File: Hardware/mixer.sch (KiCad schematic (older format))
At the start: 0 parts

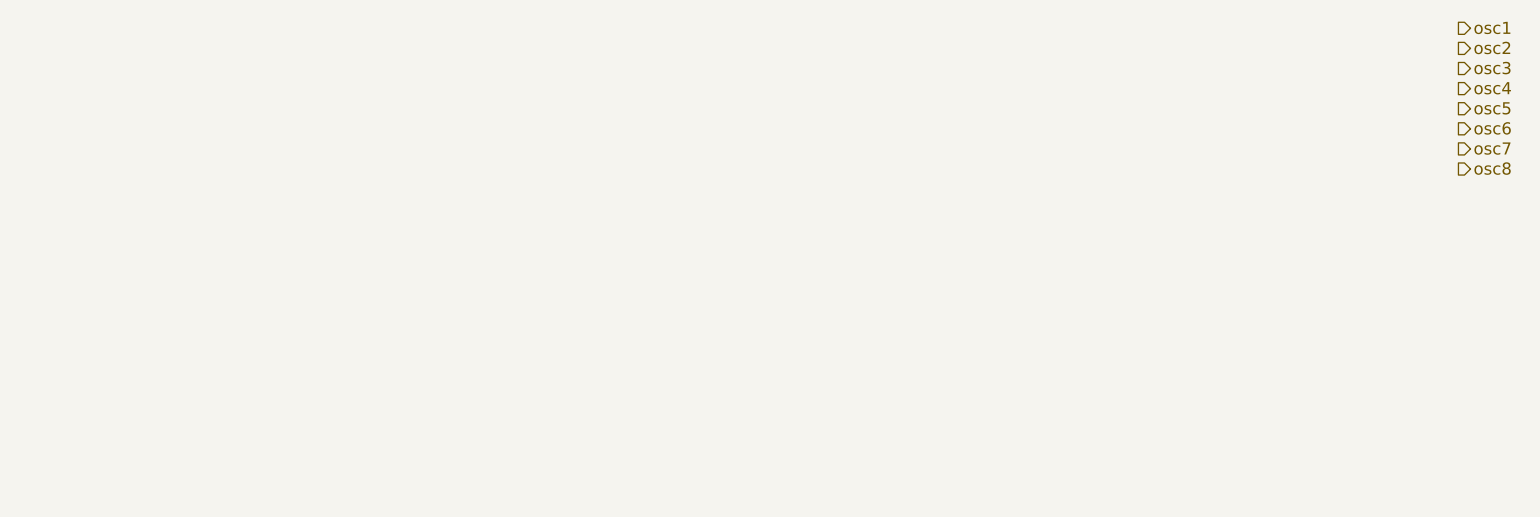
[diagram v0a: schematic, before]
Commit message: add sheets for the remaining functionality. This should hopefully be all sheets, but might add more if necessary.
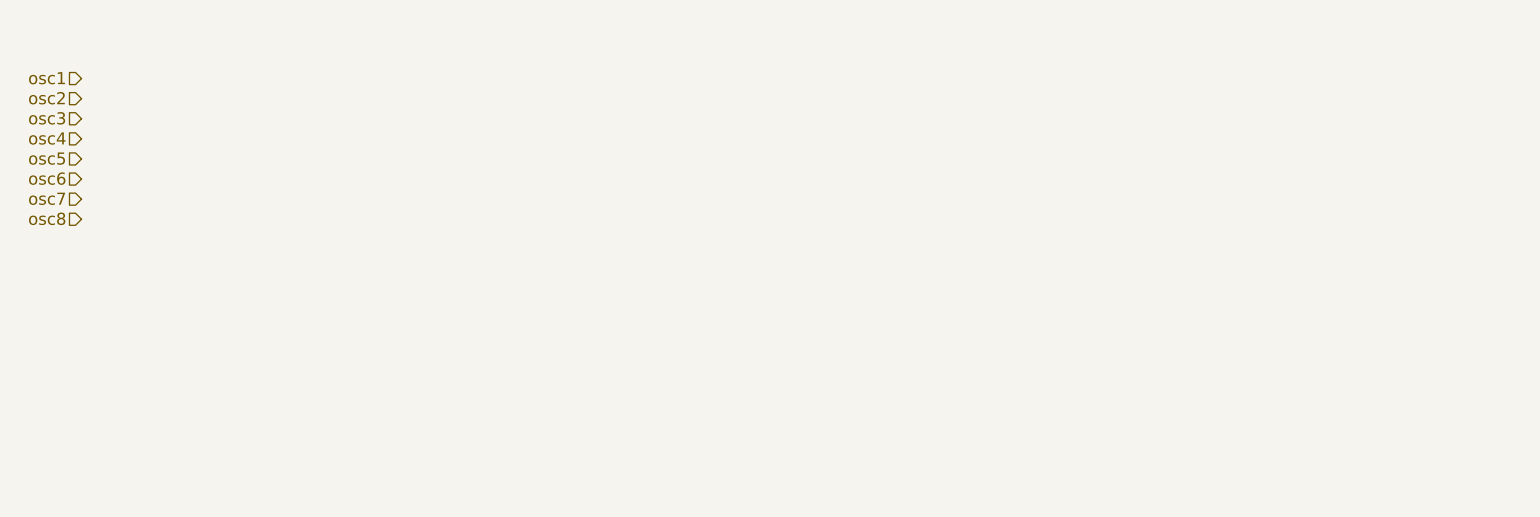
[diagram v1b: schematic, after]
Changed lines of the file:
@@
 $Descr A4 11693 8268
 encoding utf-8
-Sheet 2 7
+Sheet 6 7
 Title ""
 Date ""
@@
 Comment4 ""
 $EndDescr
-Text HLabel 9050 1900 2    60   Output ~ 0
+Text HLabel 2200 2150 0    60   Input ~ 0
 osc1
-Text HLabel 9050 2000 2    60   Output ~ 0
+Text HLabel 2200 2250 0    60   Input ~ 0
 osc2
-Text HLabel 9050 2100 2    60   Output ~ 0
+Text HLabel 2200 2350 0    60   Input ~ 0
 osc3
-Text HLabel 9050 2200 2    60   Output ~ 0
+Text HLabel 2200 2450 0    60   Input ~ 0
 osc4
-Text HLabel 9050 2300 2    60   Output ~ 0
+Text HLabel 2200 2550 0    60   Input ~ 0
 osc5
-Text HLabel 9050 2400 2    60   Output ~ 0
+Text HLabel 2200 2650 0    60   Input ~ 0
 osc6
-Text HLabel 9050 2500 2    60   Output ~ 0
+Text HLabel 2200 2750 0    60   Input ~ 0
 osc7
-Text HLabel 9050 2600 2    60   Output ~ 0
+Text HLabel 2200 2850 0    60   Input ~ 0
 osc8
 $EndSCHEMATC

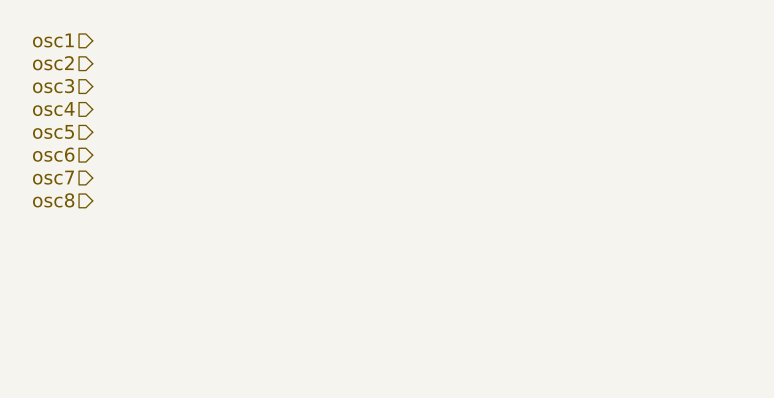
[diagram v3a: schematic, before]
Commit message: add bill of materials spreadsheet and begin to populate with values
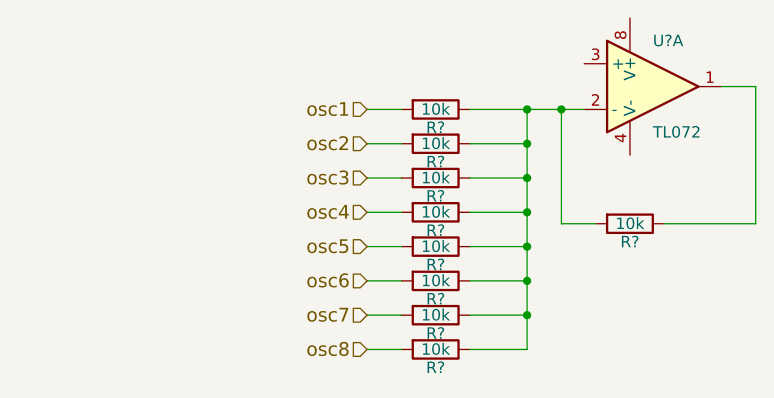
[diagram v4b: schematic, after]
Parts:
- added R? (x9): 10k, symbol R
- added U?: TL072, symbol TL072
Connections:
- net osc1: now also R?.2
- net osc2: now also R?.2
- net osc3: now also R?.2
- net osc4: now also R?.2
- net osc5: now also R?.2
- net osc6: now also R?.2
- net osc7: now also R?.2
- net osc8: now also R?.2
- new net: R?.1, R?.1, R?.1, R?.1, R?.1, R?.1, R?.1, R?.1, R?.2, U?.2 (-)
- new net: R?.1, U?.1
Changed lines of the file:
@@
 Comment4 ""
 $EndDescr
-Text HLabel 2200 2150 0    60   Input ~ 0
+Text HLabel 3400 2450 0    60   Input ~ 0
 osc1
-Text HLabel 2200 2250 0    60   Input ~ 0
+Text HLabel 3400 2600 0    60   Input ~ 0
 osc2
-Text HLabel 2200 2350 0    60   Input ~ 0
+Text HLabel 3400 2750 0    60   Input ~ 0
 osc3
-Text HLabel 2200 2450 0    60   Input ~ 0
+Text HLabel 3400 2900 0    60   Input ~ 0
 osc4
-Text HLabel 2200 2550 0    60   Input ~ 0
+Text HLabel 3400 3050 0    60   Input ~ 0
 osc5
-Text HLabel 2200 2650 0    60   Input ~ 0
+Text HLabel 3400 3200 0    60   Input ~ 0
 osc6
-Text HLabel 2200 2750 0    60   Input ~ 0
+Text HLabel 3400 3350 0    60   Input ~ 0
 osc7
-Text HLabel 2200 2850 0    60   Input ~ 0
+Text HLabel 3400 3500 0    60   Input ~ 0
 osc8
+$Comp
+L R R?
+U 1 1 5C368A69
+P 3700 2450
+F 0 "R?" V 3780 2450 50  0000 C CNN
+F 1 "10k" V 3700 2450 50  0000 C CNN
+F 2 "" V 3630 2450 50  0001 C CNN
+F 3 "" H 3700 2450 50  0001 C CNN
+	1    3700 2450
+	0    1    1    0
+$EndComp
+$Comp
+L R R?
+U 1 1 5C368B13
+P 3700 2600
+F 0 "R?" V 3780 2600 50  0000 C CNN
+F 1 "10k" V 3700 2600 50  0000 C CNN
+F 2 "" V 3630 2600 50  0001 C CNN
+F 3 "" H 3700 2600 50  0001 C CNN
+	1    3700 2600
+	0    1    1    0
+$EndComp
+$Comp
+L R R?
+U 1 1 5C368B2B
+P 3700 2750
+F 0 "R?" V 3780 2750 50  0000 C CNN
+F 1 "10k" V 3700 2750 50  0000 C CNN
+F 2 "" V 3630 2750 50  0001 C CNN
+F 3 "" H 3700 2750 50  0001 C CNN
+	1    3700 2750
+	0    1    1    0
+$EndComp
+$Comp
+L R R?
+U 1 1 5C368B46
+P 3700 2900
+F 0 "R?" V 3780 2900 50  0000 C CNN
+F 1 "10k" V 3700 2900 50  0000 C CNN
+F 2 "" V 3630 2900 50  0001 C CNN
+F 3 "" H 3700 2900 50  0001 C CNN
+	1    3700 2900
+	0    1    1    0
+$EndComp
+$Comp
+L R R?
+U 1 1 5C368B64
+P 3700 3050
+F 0 "R?" V 3780 3050 50  0000 C CNN
+F 1 "10k" V 3700 3050 50  0000 C CNN
+F 2 "" V 3630 3050 50  0001 C CNN
+F 3 "" H 3700 3050 50  0001 C CNN
+	1    3700 3050
+	0    1    1    0
+$EndComp
+$Comp
+L R R?
+U 1 1 5C368B85
+P 3700 3200
+F 0 "R?" V 3780 3200 50  0000 C CNN
+F 1 "10k" V 3700 3200 50  0000 C CNN
+F 2 "" V 3630 3200 50  0001 C CNN
+F 3 "" H 3700 3200 50  0001 C CNN
+	1    3700 3200
+	0    1    1    0
+$EndComp
+$Comp
+L R R?
+U 1 1 5C368BA9
+P 3700 3350
+F 0 "R?" V 3780 3350 50  0000 C CNN
+F 1 "10k" V 3700 3350 50  0000 C CNN
+F 2 "" V 3630 3350 50  0001 C CNN
+F 3 "" H 3700 3350 50  0001 C CNN
+	1    3700 3350
+	0    1    1    0
+$EndComp
+$Comp
+L R R?
+U 1 1 5C368BD0
+P 3700 3500
+F 0 "R?" V 3780 3500 50  0000 C CNN
+F 1 "10k" V 3700 3500 50  0000 C CNN
+F 2 "" V 3630 3500 50  0001 C CNN
+F 3 "" H 3700 3500 50  0001 C CNN
+	1    3700 3500
+	0    1    1    0
+$EndComp
+Wire Wire Line
+	3400 2450 3550 2450
+Wire Wire Line
+	3400 2600 3550 2600
+Wire Wire Line
+	3400 2750 3550 2750
+Wire Wire Line
+	3400 2900 3550 2900
+Wire Wire Line
+	3400 3050 3550 3050
+Wire Wire Line
+	3400 3200 3550 3200
+Wire Wire Line
+	3400 3350 3550 3350
+Wire Wire Line
+	3400 3500 3550 3500
+$Comp
+L TL072 U?
+U 1 1 5C368C88
+P 4650 2350
+F 0 "U?" H 4650 2550 50  0000 L CNN
+F 1 "TL072" H 4650 2150 50  0000 L CNN
+F 2 "" H 4650 2350 50  0001 C CNN
+F 3 "" H 4650 2350 50  0001 C CNN
+	1    4650 2350
+	1    0    0    -1
+$EndComp
+$Comp
+L R R?
+U 1 1 5C368D28
+P 4550 2950
+F 0 "R?" V 4630 2950 50  0000 C CNN
+F 1 "10k" V 4550 2950 50  0000 C CNN
+F 2 "" V 4480 2950 50  0001 C CNN
+F 3 "" H 4550 2950 50  0001 C CNN
+	1    4550 2950
+	0    1    1    0
+$EndComp
+Wire Wire Line
+	4700 2950 5100 2950
+Wire Wire Line
+	5100 2950 5100 2350
+Wire Wire Line
+	5100 2350 4950 2350
+Wire Wire Line
+	4400 2950 4250 2950
+Wire Wire Line
+	4250 2950 4250 2450
+Wire Wire Line
+	3850 2450 4350 2450
+Wire Wire Line
+	3850 3500 4100 3500
+Connection ~ 4250 2450
+Wire Wire Line
+	3850 3350 4100 3350
+Connection ~ 4100 3350
+Wire Wire Line
+	3850 3200 4100 3200
+Connection ~ 4100 3200
+Wire Wire Line
+	3850 3050 4100 3050
+Connection ~ 4100 3050
+Wire Wire Line
+	3850 2900 4100 2900
+Connection ~ 4100 2900
+Wire Wire Line
+	3850 2600 4100 2600
+Connection ~ 4100 2600
+Connection ~ 4100 2450
+Wire Wire Line
+	4100 3500 4100 2450
+Wire Wire Line
+	3850 2750 4100 2750
+Connection ~ 4100 2750
 $EndSCHEMATC

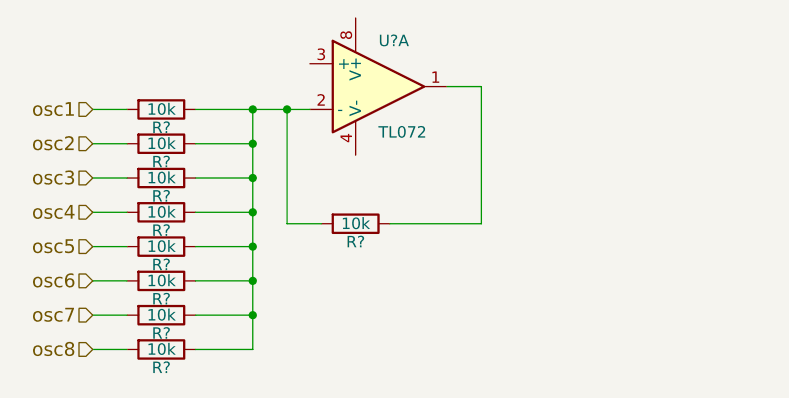
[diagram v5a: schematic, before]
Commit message: complete wiring of top level schematic hierarchical pages
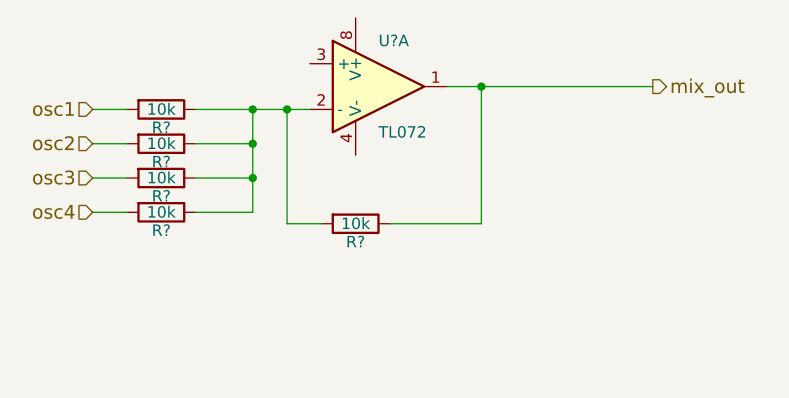
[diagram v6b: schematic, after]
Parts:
- removed R? (x4): 10k, symbol R
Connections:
- net mix_out: now reaches R?.1, U?.1
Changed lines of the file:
@@
 $Descr A4 11693 8268
 encoding utf-8
-Sheet 6 8
+Sheet 5 8
 Title ""
 Date ""
@@
 Text HLabel 3400 2900 0    60   Input ~ 0
 osc4
-Text HLabel 3400 3050 0    60   Input ~ 0
-osc5
-Text HLabel 3400 3200 0    60   Input ~ 0
-osc6
-Text HLabel 3400 3350 0    60   Input ~ 0
-osc7
-Text HLabel 3400 3500 0    60   Input ~ 0
-osc8
 $Comp
 L R R?
@@
 	0    1    1    0
 $EndComp
-$Comp
-L R R?
-U 1 1 5C368B64
-P 3700 3050
-F 0 "R?" V 3780 3050 50  0000 C CNN
-F 1 "10k" V 3700 3050 50  0000 C CNN
-F 2 "" V 3630 3050 50  0001 C CNN
-F 3 "" H 3700 3050 50  0001 C CNN
-	1    3700 3050
-	0    1    1    0
-$EndComp
-$Comp
-L R R?
-U 1 1 5C368B85
-P 3700 3200
-F 0 "R?" V 3780 3200 50  0000 C CNN
-F 1 "10k" V 3700 3200 50  0000 C CNN
-F 2 "" V 3630 3200 50  0001 C CNN
-F 3 "" H 3700 3200 50  0001 C CNN
-	1    3700 3200
-	0    1    1    0
-$EndComp
-$Comp
-L R R?
-U 1 1 5C368BA9
-P 3700 3350
-F 0 "R?" V 3780 3350 50  0000 C CNN
-F 1 "10k" V 3700 3350 50  0000 C CNN
-F 2 "" V 3630 3350 50  0001 C CNN
-F 3 "" H 3700 3350 50  0001 C CNN
-	1    3700 3350
-	0    1    1    0
-$EndComp
-$Comp
-L R R?
-U 1 1 5C368BD0
-P 3700 3500
-F 0 "R?" V 3780 3500 50  0000 C CNN
-F 1 "10k" V 3700 3500 50  0000 C CNN
-F 2 "" V 3630 3500 50  0001 C CNN
-F 3 "" H 3700 3500 50  0001 C CNN
-	1    3700 3500
-	0    1    1    0
-$EndComp
 Wire Wire Line
 	3400 2450 3550 2450
@@
 Wire Wire Line
 	3400 2900 3550 2900
-Wire Wire Line
-	3400 3050 3550 3050
-Wire Wire Line
-	3400 3200 3550 3200
-Wire Wire Line
-	3400 3350 3550 3350
-Wire Wire Line
-	3400 3500 3550 3500
 $Comp
 L TL072 U?
@@
 	5100 2950 5100 2350
 Wire Wire Line
-	5100 2350 4950 2350
+	4950 2350 5850 2350
 Wire Wire Line
 	4400 2950 4250 2950
@@
 Wire Wire Line
 	3850 2450 4350 2450
-Wire Wire Line
-	3850 3500 4100 3500
 Connection ~ 4250 2450
 Wire Wire Line
-	3850 3350 4100 3350
-Connection ~ 4100 3350
-Wire Wire Line
-	3850 3200 4100 3200
-Connection ~ 4100 3200
-Wire Wire Line
-	3850 3050 4100 3050
-Connection ~ 4100 3050
-Wire Wire Line
 	3850 2900 4100 2900
-Connection ~ 4100 2900
 Wire Wire Line
 	3850 2600 4100 2600
@@
 Connection ~ 4100 2450
 Wire Wire Line
-	4100 3500 4100 2450
-Wire Wire Line
 	3850 2750 4100 2750
 Connection ~ 4100 2750
+Wire Wire Line
+	4100 2900 4100 2450
+Text HLabel 5850 2350 2    60   Output ~ 0
+mix_out
+Connection ~ 5100 2350
 $EndSCHEMATC

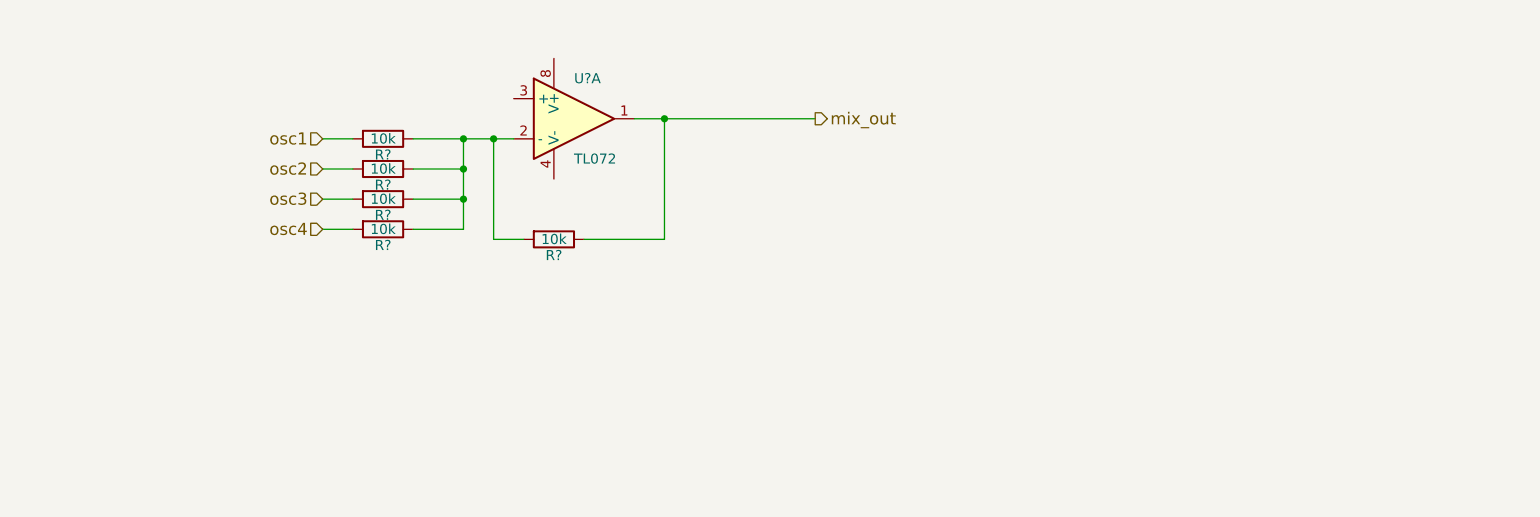
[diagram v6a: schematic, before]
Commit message: add power jack, 3.3V regulator, VREF divider
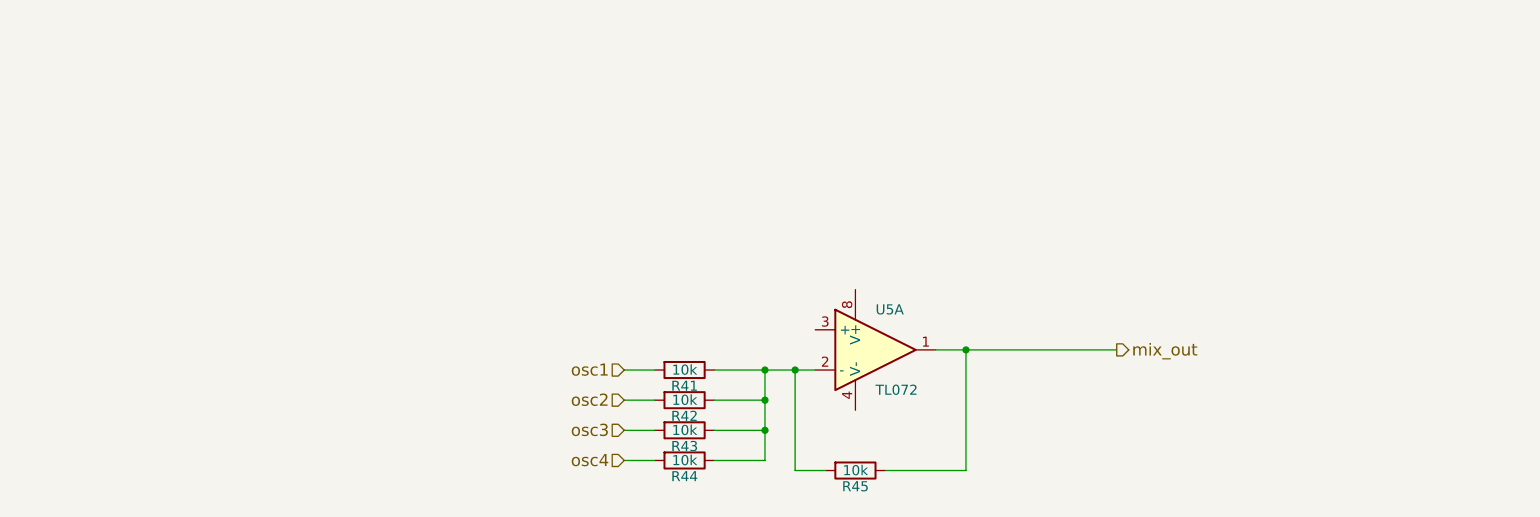
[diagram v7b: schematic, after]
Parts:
- gave numbers to parts that had none: 6
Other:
- moved on the sheet: R41, R42, R43, R44, R45, U5A
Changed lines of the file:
@@
 Comment4 ""
 $EndDescr
-Text HLabel 3400 2450 0    60   Input ~ 0
+Text HLabel 4900 3600 0    60   Input ~ 0
 osc1
-Text HLabel 3400 2600 0    60   Input ~ 0
+Text HLabel 4900 3750 0    60   Input ~ 0
 osc2
-Text HLabel 3400 2750 0    60   Input ~ 0
+Text HLabel 4900 3900 0    60   Input ~ 0
 osc3
-Text HLabel 3400 2900 0    60   Input ~ 0
+Text HLabel 4900 4050 0    60   Input ~ 0
 osc4
 $Comp
-L R R?
+L R R41
 U 1 1 5C368A69
-P 3700 2450
-F 0 "R?" V 3780 2450 50  0000 C CNN
-F 1 "10k" V 3700 2450 50  0000 C CNN
-F 2 "" V 3630 2450 50  0001 C CNN
-F 3 "" H 3700 2450 50  0001 C CNN
-	1    3700 2450
+P 5200 3600
+F 0 "R41" V 5280 3600 50  0000 C CNN
+F 1 "10k" V 5200 3600 50  0000 C CNN
+F 2 "" V 5130 3600 50  0001 C CNN
+F 3 "" H 5200 3600 50  0001 C CNN
+	1    5200 3600
 	0    1    1    0
 $EndComp
 $Comp
-L R R?
+L R R42
 U 1 1 5C368B13
-P 3700 2600
-F 0 "R?" V 3780 2600 50  0000 C CNN
-F 1 "10k" V 3700 2600 50  0000 C CNN
-F 2 "" V 3630 2600 50  0001 C CNN
-F 3 "" H 3700 2600 50  0001 C CNN
-	1    3700 2600
+P 5200 3750
+F 0 "R42" V 5280 3750 50  0000 C CNN
+F 1 "10k" V 5200 3750 50  0000 C CNN
+F 2 "" V 5130 3750 50  0001 C CNN
+F 3 "" H 5200 3750 50  0001 C CNN
+	1    5200 3750
 	0    1    1    0
 $EndComp
 $Comp
-L R R?
+L R R43
 U 1 1 5C368B2B
-P 3700 2750
-F 0 "R?" V 3780 2750 50  0000 C CNN
-F 1 "10k" V 3700 2750 50  0000 C CNN
-F 2 "" V 3630 2750 50  0001 C CNN
-F 3 "" H 3700 2750 50  0001 C CNN
-	1    3700 2750
+P 5200 3900
+F 0 "R43" V 5280 3900 50  0000 C CNN
+F 1 "10k" V 5200 3900 50  0000 C CNN
+F 2 "" V 5130 3900 50  0001 C CNN
+F 3 "" H 5200 3900 50  0001 C CNN
+	1    5200 3900
 	0    1    1    0
 $EndComp
 $Comp
-L R R?
+L R R44
 U 1 1 5C368B46
-P 3700 2900
-F 0 "R?" V 3780 2900 50  0000 C CNN
-F 1 "10k" V 3700 2900 50  0000 C CNN
-F 2 "" V 3630 2900 50  0001 C CNN
-F 3 "" H 3700 2900 50  0001 C CNN
-	1    3700 2900
+P 5200 4050
+F 0 "R44" V 5280 4050 50  0000 C CNN
+F 1 "10k" V 5200 4050 50  0000 C CNN
+F 2 "" V 5130 4050 50  0001 C CNN
+F 3 "" H 5200 4050 50  0001 C CNN
+	1    5200 4050
 	0    1    1    0
 $EndComp
 Wire Wire Line
-	3400 2450 3550 2450
+	4900 3600 5050 3600
 Wire Wire Line
-	3400 2600 3550 2600
+	4900 3750 5050 3750
 Wire Wire Line
-	3400 2750 3550 2750
+	4900 3900 5050 3900
 Wire Wire Line
-	3400 2900 3550 2900
+	4900 4050 5050 4050
 $Comp
-L TL072 U?
+L TL072 U5
 U 1 1 5C368C88
-P 4650 2350
-F 0 "U?" H 4650 2550 50  0000 L CNN
-F 1 "TL072" H 4650 2150 50  0000 L CNN
-F 2 "" H 4650 2350 50  0001 C CNN
-F 3 "" H 4650 2350 50  0001 C CNN
-	1    4650 2350
+P 6150 3500
+F 0 "U5" H 6150 3700 50  0000 L CNN
+F 1 "TL072" H 6150 3300 50  0000 L CNN
+F 2 "" H 6150 3500 50  0001 C CNN
+F 3 "" H 6150 3500 50  0001 C CNN
+	1    6150 3500
 	1    0    0    -1
 $EndComp
 $Comp
-L R R?
+L R R45
 U 1 1 5C368D28
-P 4550 2950
-F 0 "R?" V 4630 2950 50  0000 C CNN
-F 1 "10k" V 4550 2950 50  0000 C CNN
-F 2 "" V 4480 2950 50  0001 C CNN
-F 3 "" H 4550 2950 50  0001 C CNN
-	1    4550 2950
+P 6050 4100
+F 0 "R45" V 6130 4100 50  0000 C CNN
+F 1 "10k" V 6050 4100 50  0000 C CNN
+F 2 "" V 5980 4100 50  0001 C CNN
+F 3 "" H 6050 4100 50  0001 C CNN
+	1    6050 4100
 	0    1    1    0
 $EndComp
 Wire Wire Line
-	4700 2950 5100 2950
+	6200 4100 6600 4100
 Wire Wire Line
-	5100 2950 5100 2350
+	6600 4100 6600 3500
 Wire Wire Line
-	4950 2350 5850 2350
+	6450 3500 7350 3500
 Wire Wire Line
-	4400 2950 4250 2950
+	5900 4100 5750 4100
 Wire Wire Line
-	4250 2950 4250 2450
+	5750 4100 5750 3600
 Wire Wire Line
-	3850 2450 4350 2450
-Connection ~ 4250 2450
+	5350 3600 5850 3600
+Connection ~ 5750 3600
 Wire Wire Line
-	3850 2900 4100 2900
+	5350 4050 5600 4050
 Wire Wire Line
-	3850 2600 4100 2600
-Connection ~ 4100 2600
-Connection ~ 4100 2450
+	5350 3750 5600 3750
+Connection ~ 5600 3750
+Connection ~ 5600 3600
 Wire Wire Line
-	3850 2750 4100 2750
-Connection ~ 4100 2750
+	5350 3900 5600 3900
+Connection ~ 5600 3900
 Wire Wire Line
-	4100 2900 4100 2450
-Text HLabel 5850 2350 2    60   Output ~ 0
+	5600 4050 5600 3600
+Text HLabel 7350 3500 2    60   Output ~ 0
 mix_out
-Connection ~ 5100 2350
+Connection ~ 6600 3500
 $EndSCHEMATC
